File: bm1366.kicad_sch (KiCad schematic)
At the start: 44 parts, among them J3 Conn_01x05, Q3 BSS138, Q4 BSS138, Q5 BSS138, U14 BM1366_mode1, U2 +0V8, U4 +0V8, U5 MCP1824T-1802E, U6 MCP1824T-0802E, U7 25MHz, U8 +0V8

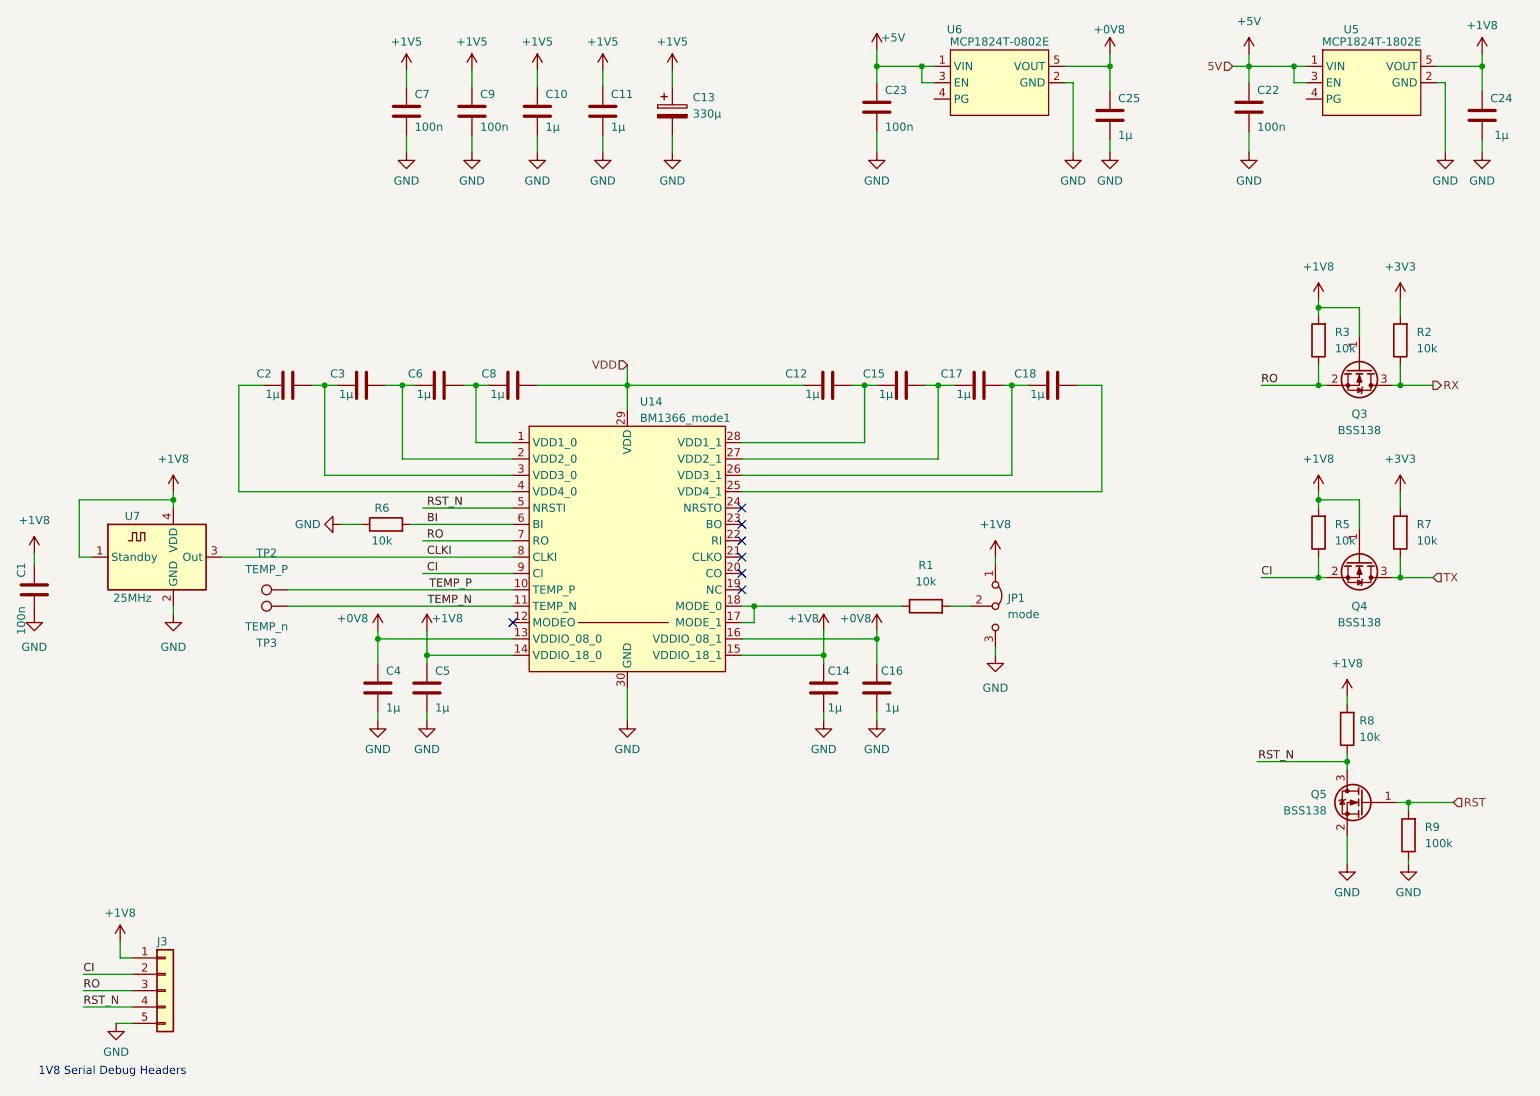
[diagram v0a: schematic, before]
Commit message: added back the two 1uF
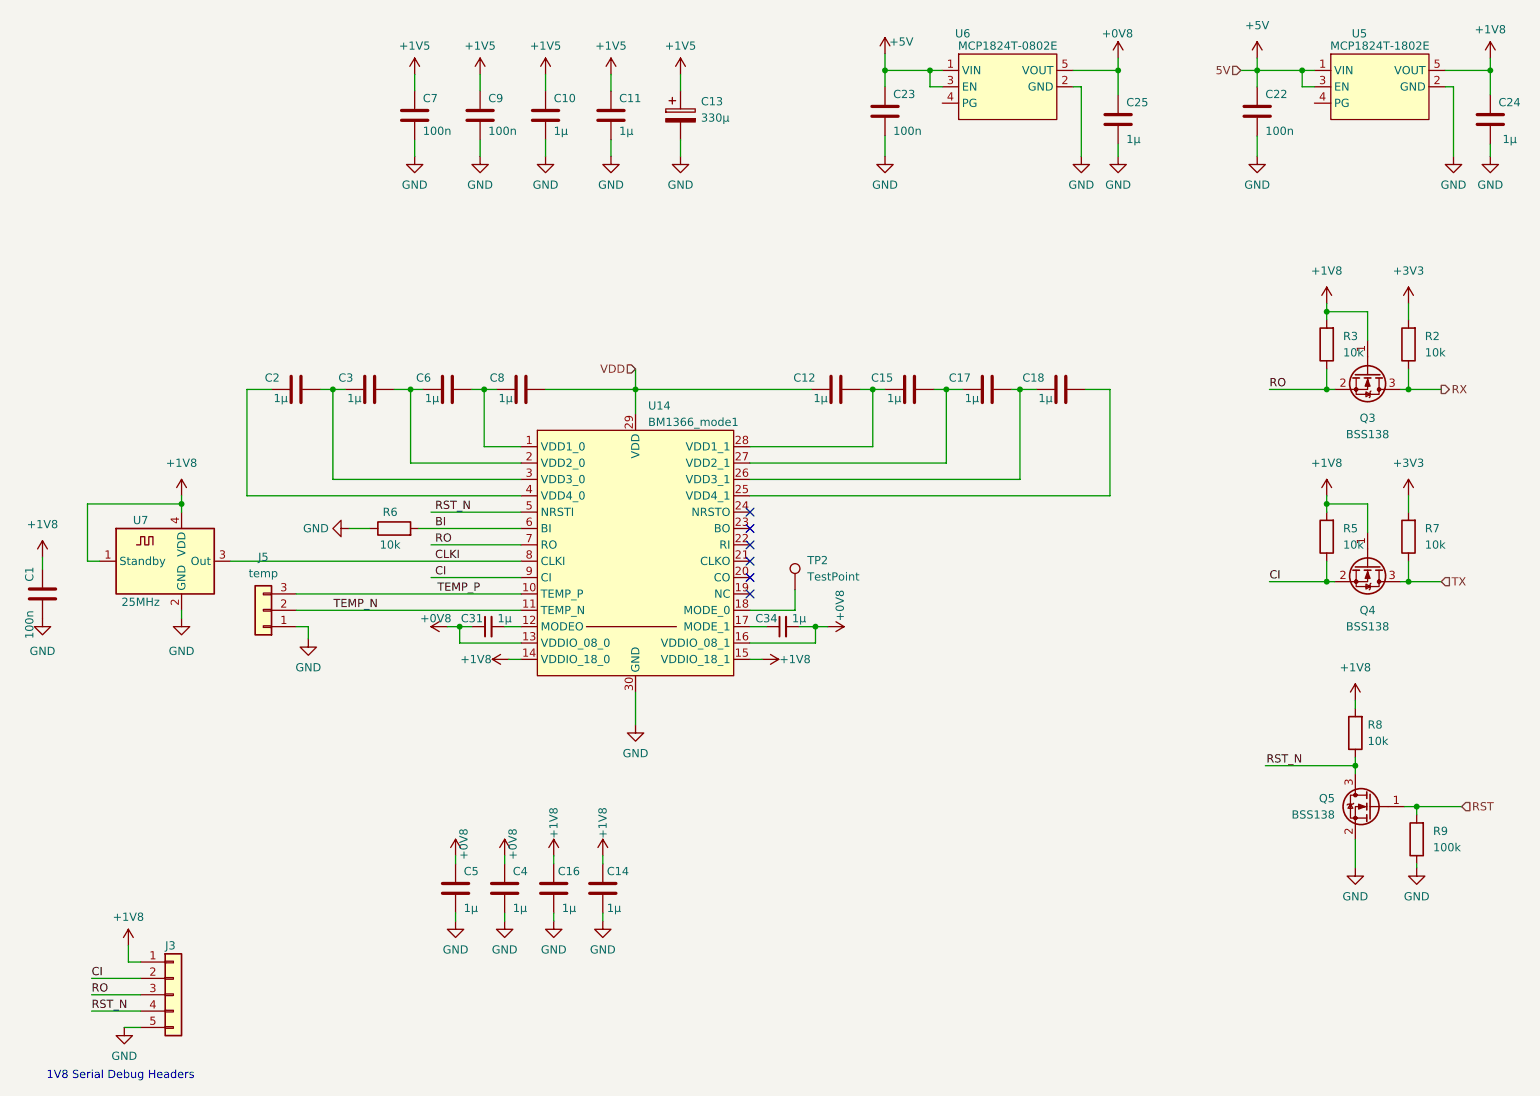
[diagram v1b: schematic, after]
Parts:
- removed JP1: mode, Jumper:SolderJumper-3_P1.3mm_Open_RoundedPad1.0x1.5mm, symbol Jumper:Jumper_3_Bridged12
- removed R1: 10k, Resistor_SMD:R_0805_2012Metric, symbol Device:R
- removed TP3: TEMP_n, TestPoint:TestPoint_Pad_D2.0mm, symbol Connector:TestPoint
- added C31, C34: 1µ, Capacitor_SMD:C_0805_2012Metric, symbol Device:C_Small
- added J5: temp, Connector_PinHeader_2.54mm:PinHeader_1x03_P2.54mm_Vertical, symbol Connector_Generic:Conn_01x03
- added U10, U9: +0V8, symbol mylib7:+0V8
- TP2: value TEMP_P -> TestPoint; Distributor - -> (none)
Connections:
- net +0V8: now also C5.1, C31.1, C34.2, U10.1 (+0V8), U9.1 (+0V8); no longer C16.1
- net +1V8: now also C16.1; no longer C5.1
- net GND: now also J5.1 (Pin_1)
- net TEMP_N: now also J5.2 (Pin_2)
- net TEMP_P: now also J5.3 (Pin_3); no longer TP2.1
- net at U14.18 (MODE_0): now also TP2.1; no longer U14.17 (MODE_1)
- net at U14.12 (MODEO): now also C31.2
- new net: C34.1, U14.17 (MODE_1)
- no-connect marks 7 -> 6
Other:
- moved on the sheet: C1, C10, C11, C12, C13, C14, C15, C16, C17, C18, C2, C22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

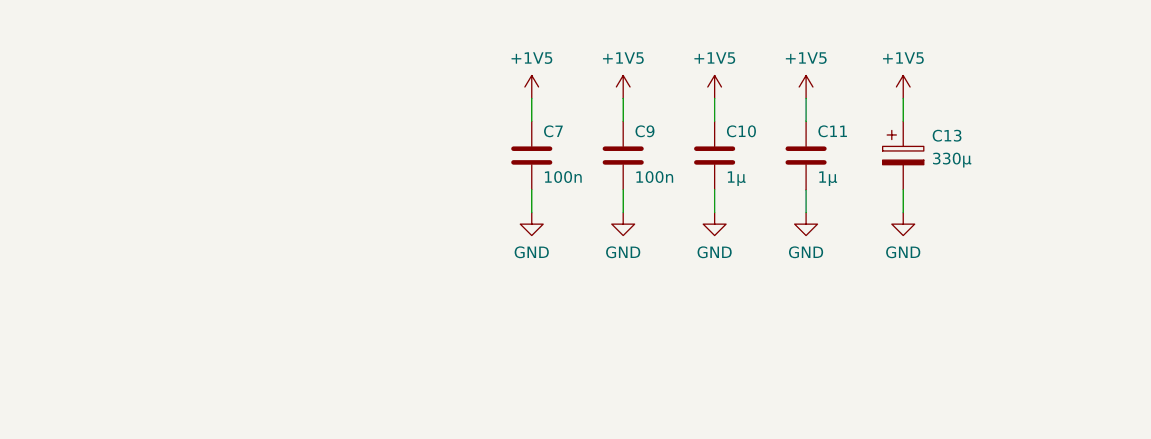
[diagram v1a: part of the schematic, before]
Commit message: removed tantal and replaced with ceramic caps
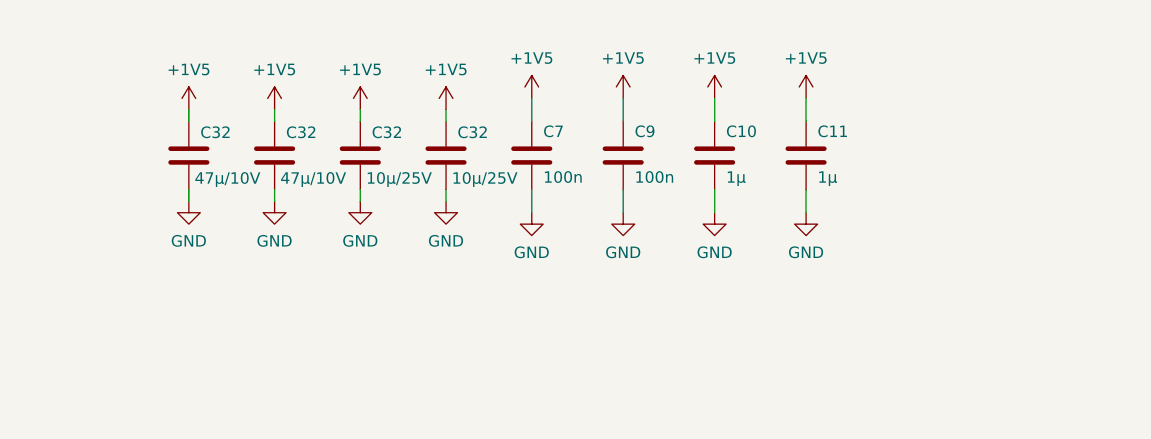
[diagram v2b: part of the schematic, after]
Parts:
- removed C13: 330µ, Capacitor_Tantalum_SMD:CP_EIA-7343-31_Kemet-D_Pad2.25x2.55mm_HandSolder, symbol Device:C_Polarized
- added C32 (x2): 47µ/10V, Capacitor_SMD:C_1206_3216Metric, symbol Device:C
- added C32 (x2): 10µ/25V, Capacitor_SMD:C_1206_3216Metric, symbol Device:C
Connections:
- net +1V5: now also C32.1, C32.1, C32.1, C32.1
- net GND: now also C32.2, C32.2, C32.2, C32.2

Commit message: revised heat-sinking. Supports heatsinks with 40x40 size with holes 35x35, 32x32 and 33x33
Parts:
- TP2: footprint TestPoint:TestPoint_Pad_D2.0mm -> TestPoint:TestPoint_Pad_D1.5mm
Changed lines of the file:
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@@
       (effects (font (size 1.27 1.27)) (justify left))
     )
-    (property "Footprint" "TestPoint:TestPoint_Pad_D2.0mm" (at 145.415 113.665 0)
+    (property "Footprint" "TestPoint:TestPoint_Pad_D1.5mm" (at 145.415 113.665 0)
       (effects (font (size 1.27 1.27)) hide)
     )

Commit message: added gerbers and bom
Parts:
- added C13, C43, C44, C45: 100n, Capacitor_SMD:C_0805_2012Metric, symbol Device:C
- added U11, U12: +0V8, symbol mylib7:+0V8
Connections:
- net +0V8: now also C13.1, C43.1, U11.1 (+0V8), U12.1 (+0V8)
- net +1V8: now also C44.1, C45.1
- net GND: now also C13.2, C43.2, C44.2, C45.2
- no-connect marks 6 -> 8
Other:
- moved on the sheet: C10, C11, C9

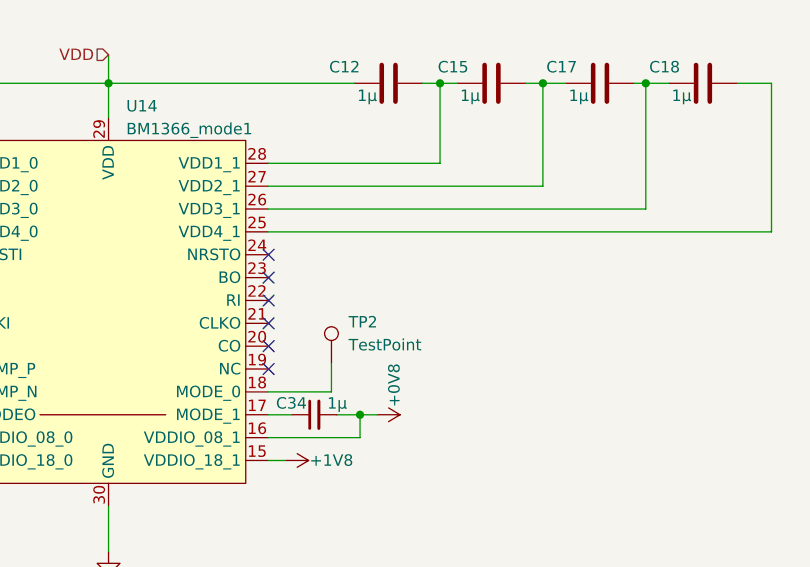
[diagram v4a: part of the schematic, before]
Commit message: fixed zone-edgecut clearance, added 2nd gnd layer and stitched them together for copper balance
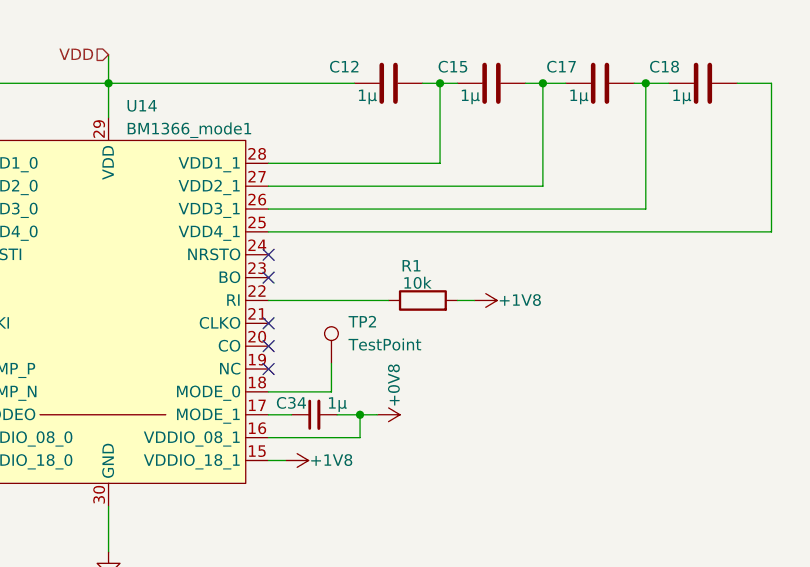
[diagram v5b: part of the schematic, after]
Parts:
- added R1: 10k, Resistor_SMD:R_0805_2012Metric, symbol Device:R
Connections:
- net +1V8: now also R1.2
- net at U14.22 (RI): now also R1.1
- no-connect marks 8 -> 7
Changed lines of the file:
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@@
   (no_connect (at 133.35 101.6))
   (no_connect (at 163.195 38.1))
-  (no_connect (at 133.35 106.68))
   (no_connect (at 133.35 109.22))
   (no_connect (at 220.98 38.1))
@@
     (stroke (width 0) (type default))
   )
+  (wire (pts (xy 154.305 106.68) (xy 156.21 106.68))
+    (stroke (width 0) (type default))
+  )
   (wire (pts (xy 30.48 100.33) (xy 30.48 109.22))
     (stroke (width 0) (type default))
@@
     (stroke (width 0) (type default))
   )
+  (wire (pts (xy 133.35 106.68) (xy 146.685 106.68))
+    (stroke (width 0) (type default))
+  )
   (wire (pts (xy 80.645 82.55) (xy 82.55 82.55))
     (stroke (width 0) (type default))
@@
     )
   )
+  (symbol (lib_id "power:+1V8") (at 156.21 106.68 270) (unit 1)
+    (in_bom yes) (on_board yes) (dnp no)
+    (property "Reference" "#PWR096" (at 152.4 106.68 0)
+      (effects (font (size 1.27 1.27)) hide)
+    )
+    (property "Value" "+1V8" (at 161.29 106.68 90)
+      (effects (font (size 1.27 1.27)))
+    )
+    (property "Footprint" "" (at 156.21 106.68 0)
+      (effects (font (size 1.27 1.27)) hide)
+    )
+    (property "Datasheet" "" (at 156.21 106.68 0)
+      (effects (font (size 1.27 1.27)) hide)
+    )
+    (pin "1")
+    (instances
+      (project "bitaxeUltra"
+        (path "/e63e39d7-6ac0-4ffd-8aa3-1841a4541b55/4cf9c075-d009-4c35-9949-adda70ae20c7"
+          (reference "#PWR096") (unit 1)
+        )
+      )
+    )
+  )
   (symbol (lib_name "GND_4") (lib_id "power:GND") (at 71.12 104.14 270) (unit 1)
     (in_bom yes) (on_board yes) (dnp no) (fields_autoplaced)
@@
         )
       )
+    )
+  )
+  (symbol (lib_id "Device:R") (at 150.495 106.68 90) (unit 1)
+    (in_bom yes) (on_board yes) (dnp no)
+    (property "Reference" "R1" (at 149.225 102.87 90)
+      (effects (font (size 1.27 1.27)))
+    )
+    (property "Value" "10k" (at 149.86 104.775 90)
+      (effects (font (size 1.27 1.27)))
+    )
+    (property "Footprint" "Resistor_SMD:R_0805_2012Metric" (at 150.495 108.458 90)
+      (effects (font (size 1.27 1.27)) hide)
+    )
+    (property "Datasheet" "~" (at 150.495 106.68 0)
+      (effects (font (size 1.27 1.27)) hide)
+    )
+    (pin "1")
+    (pin "2")
+    (instances
+      (project "bitaxeUltra"
+        (path "/e63e39d7-6ac0-4ffd-8aa3-1841a4541b55/4cf9c075-d009-4c35-9949-adda70ae20c7"
+          (reference "R1") (unit 1)
+        )
+      )

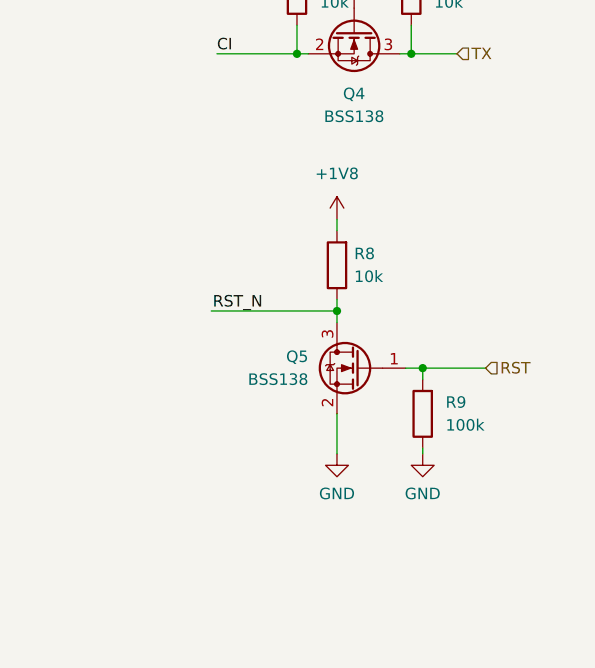
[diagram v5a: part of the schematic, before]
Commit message: fixed some order numbers, added initial python code for testing
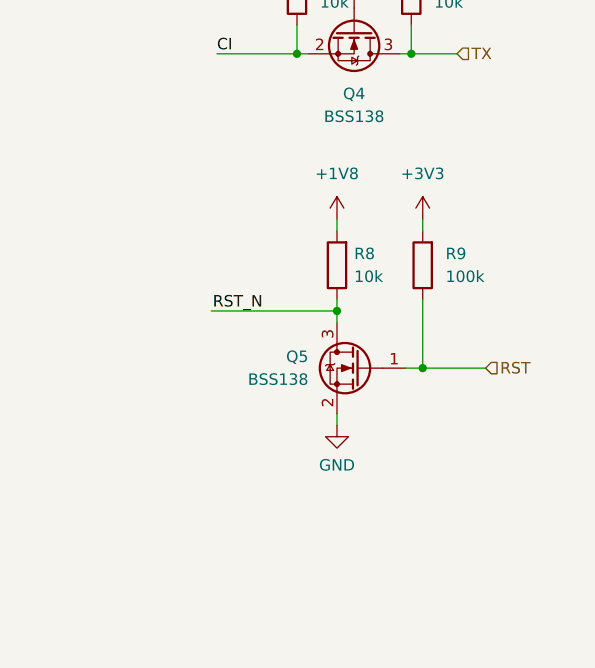
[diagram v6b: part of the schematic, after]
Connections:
- net +3V3: now also R9.2
- net GND: no longer R9.1
- net RST: now also R9.1; no longer R9.2
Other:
- moved on the sheet: R9
